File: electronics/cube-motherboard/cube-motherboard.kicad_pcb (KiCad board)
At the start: 4 copper layers, 95 x 95 mm, 58 parts, among them J1 Conn_01x02, J2 Conn_02x04_Top_Bottom, J3 Conn_02x04_Top_Bottom, J4 Conn_02x04_Top_Bottom, J5 Conn_01x18, Q1 BSS138, Q2 BSS138, U1 Escon_24/2, U2 Escon_24/2, U3 Escon_24/2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

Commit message: Organize esp32 <-> escon wiring
Remapped AO1 of M3 to an ADC1 pin.
Removed all three unused AO2 DI3 wirings and relevant diodes and capacitors
Corrected pins.h (Old version was not matching with old schematic btw)
Updated Bom accordingly
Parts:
- removed the C10 at (77.6, 96.4)
- removed the C11 at (80.2, 96.4)
- removed the C9 at (67.5, 96.4)
- removed D10, D8, D9: D_TVS, Diode_SMD:D_0402_1005Metric
- moved C8 20.3 mm to (80.1, 96.2)
- moved D7 20.3 mm to (80.1, 93.7)
- moved C7 5.17 mm to (59.9, 96.4)
- moved D6 5.11 mm to (59.9, 93.8)
- renumbered C15 to C10, C16 to C11, C14 to C9
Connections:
- C7 pad 1: AO2_M1 -> AO1_M2
- C8 pad 1: AO1_M2 -> AO1_M3
- D6 pad 2: AO2_M1 -> AO1_M2
- D7 pad 2: AO1_M2 -> AO1_M3
- U1 pad 15: DI3_M1 -> unconnected-(U1-DIO3-Pad15)
- U1 pad 19: AO2_M1 -> unconnected-(U1-AO2-Pad19)
- U2 pad 15: DI3_M2 -> unconnected-(U2-DIO3-Pad15)
- U2 pad 19: AO2_M2 -> unconnected-(U2-AO2-Pad19)
- U3 pad 15: DI3_M3 -> unconnected-(U3-DIO3-Pad15)
- U3 pad 19: AO2_M3 -> unconnected-(U3-AO2-Pad19)
- U4 pad 12: AO2_M2 -> unconnected-(U4-GPIO8/ADC1_CH7-Pad12)
- U4 pad 17: AO2_M1 -> unconnected-(U4-GPIO11/ADC2_CH0-Pad17)
- U4 pad 20: DI3_M1 -> unconnected-(U4-GPIO14/ADC2_CH3-Pad20)
- U4 pad 4: DI3_M3 -> unconnected-(U4-GPIO4/ADC1_CH3-Pad4)
- U4 pad 7: AO2_M3 -> AO1_M3
- U4 pad 8: AO1_M3 -> unconnected-(U4-GPIO15/ADC2_CH4/32K_P-Pad8)
- U4 pad 9: DI3_M2 -> unconnected-(U4-GPIO16/ADC2_CH5/32K_N-Pad9)
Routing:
- net AO2_M3: track 64.9 -> 0.00 mm
- net AO2_M2: track 55.3 -> 0.00 mm
- net AO2_M1: track 53.4 -> 0.00 mm
- net DI3_M3: track 41.6 -> 0.00 mm
- net DI3_M1: track 34.4 -> 0.00 mm
- net DI3_M2: track 34.0 -> 0.00 mm
- net GND: track 38.4 -> 30.2 mm, vias 254 -> 251
- net AO1_M3: track 67.6 -> 66.5 mm

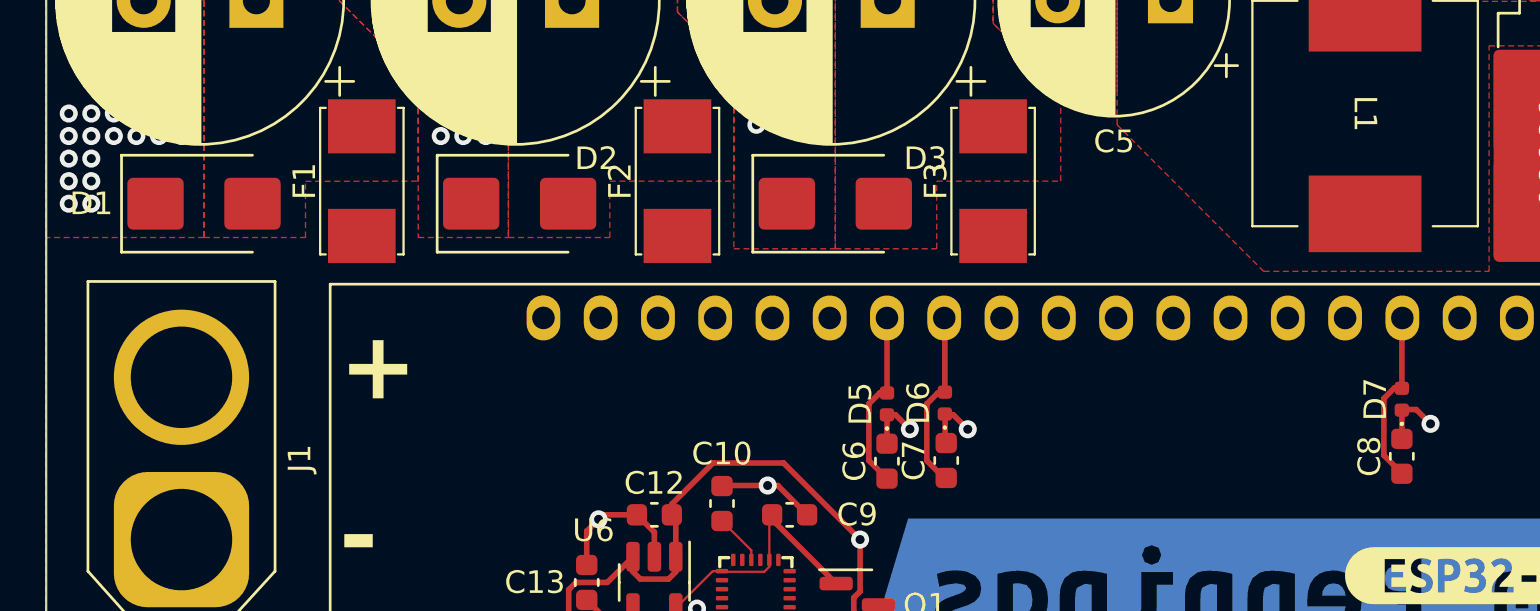
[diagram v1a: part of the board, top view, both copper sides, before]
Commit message: Fix symbol, footprint and orientation of D1,D2 and D3 diodes
Add missing 3D models for L1 & F1,F2,F3
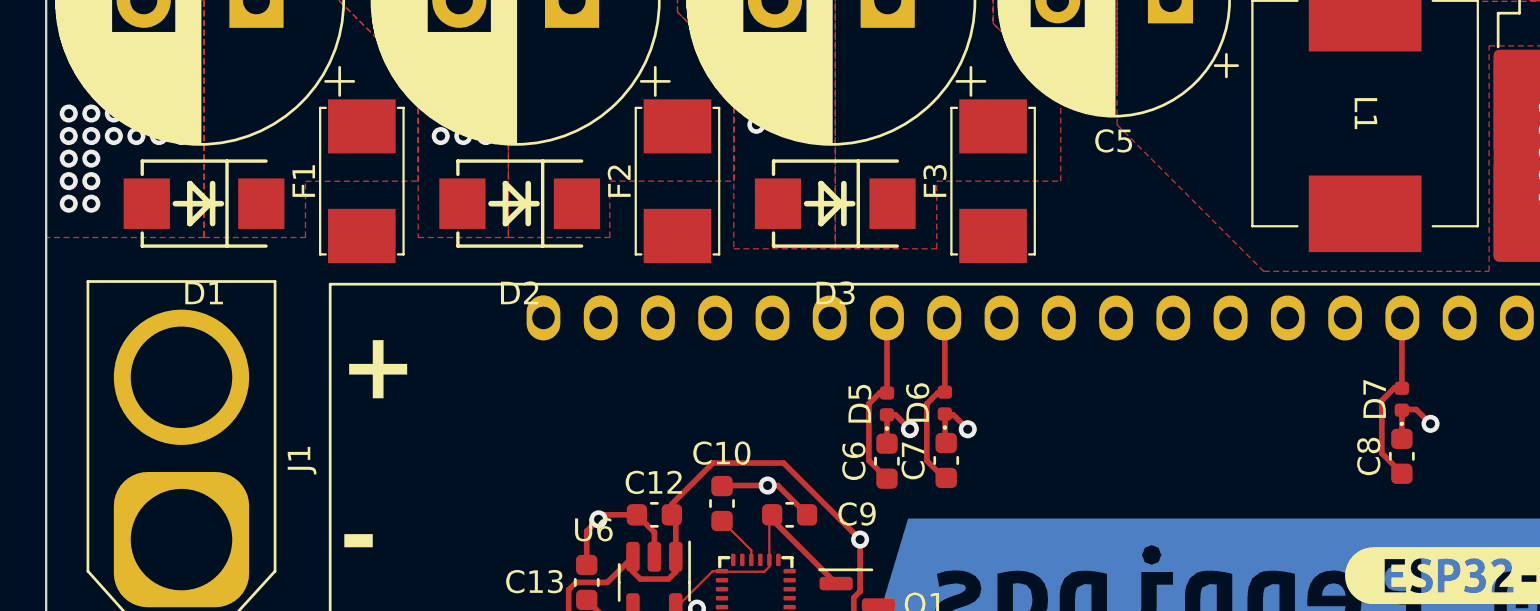
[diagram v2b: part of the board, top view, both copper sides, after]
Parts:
- D1, D2, D3: value D_TVS -> SMBJ33A; footprint Diode_SMD:D_SMB -> cube-motherboard:SMB_L4.4-W3.6-LS5.4-RD
- turned D1 to 180 degrees
- turned D2 to 180 degrees
- turned D3 to 180 degrees
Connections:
- D1 pad 1: GND -> VCC_M1
- D1 pad 2: VCC_M1 -> GND
- D2 pad 1: GND -> VCC_M2
- D2 pad 2: VCC_M2 -> GND
- D3 pad 1: GND -> VCC_M3
- D3 pad 2: VCC_M3 -> GND

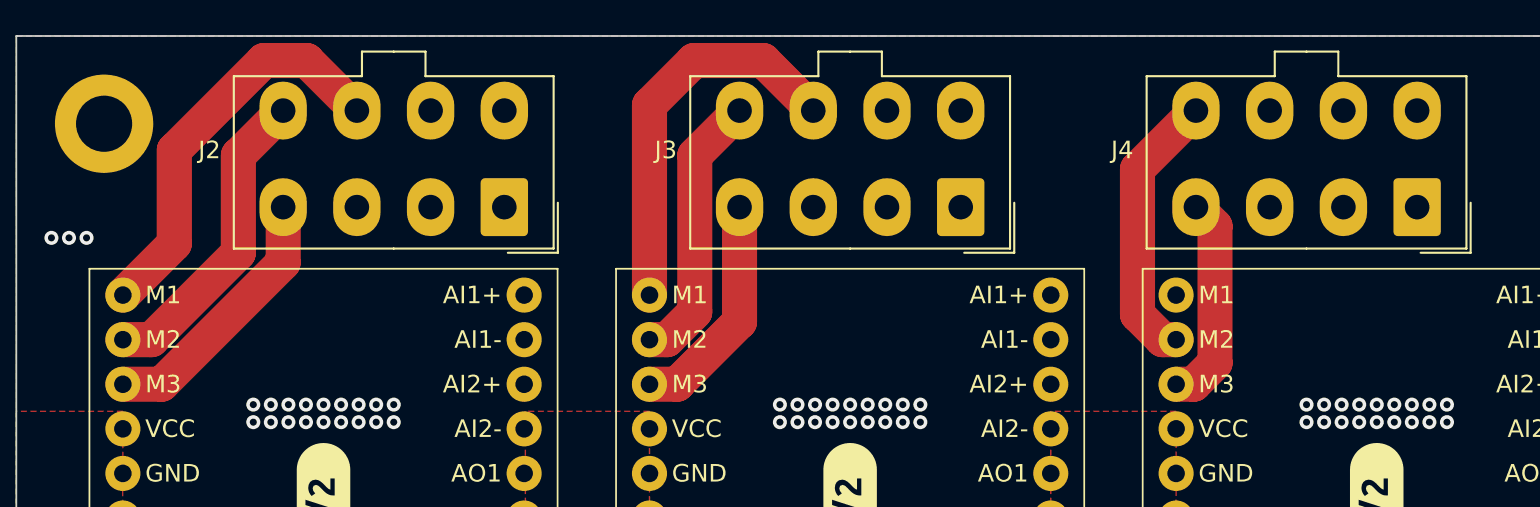
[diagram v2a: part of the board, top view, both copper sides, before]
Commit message: Remove the requirement to remap the pins of the molex cables by reorganizing pin order
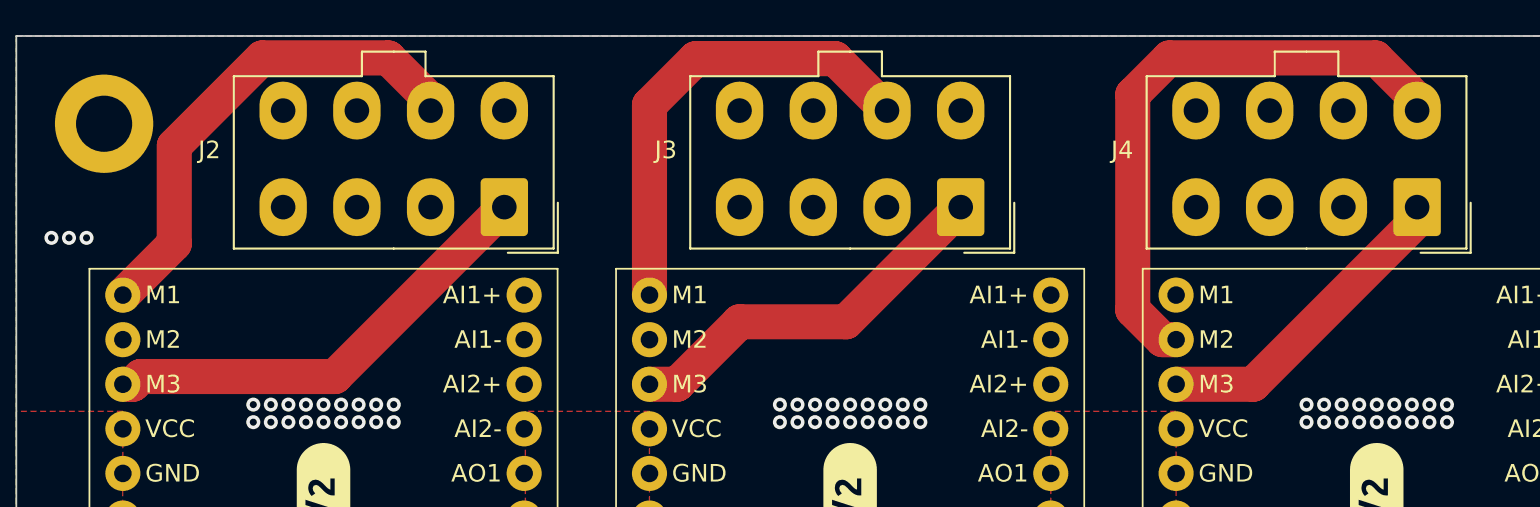
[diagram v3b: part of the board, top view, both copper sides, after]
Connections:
- J2 pad 1: H1_M1 -> P3_M1
- J2 pad 2: H2_M1 -> 5V_M1
- J2 pad 3: 5V_M1 -> H2_M1
- J2 pad 4: P3_M1 -> H1_M1
- J2 pad 5: H3_M1 -> P2_M1
- J2 pad 6: GND -> P1_M1
- J2 pad 7: P1_M1 -> GND
- J2 pad 8: P2_M1 -> H3_M1
- J3 pad 1: H1_M2 -> P3_M2
- J3 pad 2: H2_M2 -> 5V_M2
- J3 pad 3: 5V_M2 -> H2_M2
- J3 pad 4: P3_M2 -> H1_M2
- J3 pad 5: H3_M2 -> P2_M2
- J3 pad 6: GND -> P1_M2
- J3 pad 7: P1_M2 -> GND
- J3 pad 8: P2_M2 -> H3_M2
- J4 pad 1: H1_M3 -> P3_M3
- J4 pad 2: H2_M3 -> 5V_M3
- J4 pad 3: 5V_M3 -> H2_M3
- J4 pad 4: P3_M3 -> H1_M3
- J4 pad 5: H3_M3 -> P2_M3
- J4 pad 6: GND -> P1_M3
- J4 pad 7: P1_M3 -> GND
- J4 pad 8: P2_M3 -> H3_M3
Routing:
- net P2_M3: track 15.8 -> 34.1 mm
- net P2_M1: track 17.8 -> 35.3 mm
- net P2_M2: track 15.8 -> 31.9 mm
- net 5V_M1: track 23.2 -> 34.2 mm
- net P3_M1: track 15.2 -> 25.9 mm
- net H1_M2: track 32.7 -> 22.7 mm
- net H1_M1: track 34.3 -> 24.4 mm
- net P3_M2: track 13.1 -> 21.9 mm
- net 5V_M3: track 19.9 -> 28.2 mm
- net H3_M1: track 44.2 -> 36.2 mm
- net H3_M3: track 40.9 -> 33.0 mm
- net P3_M3: track 12.0 -> 18.3 mm
- net P1_M1: track 23.2 -> 28.0 mm
- net P1_M2: track 22.4 -> 26.7 mm
- net H1_M3: track 25.9 -> 21.7 mm
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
